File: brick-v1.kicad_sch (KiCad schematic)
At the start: 15 parts, among them J1 battery_header, U1 XBEE S2C PRO, U2 esp32, U3 L7805, U4 ULTRASONIC SENSOR, U5 Teensy4.1

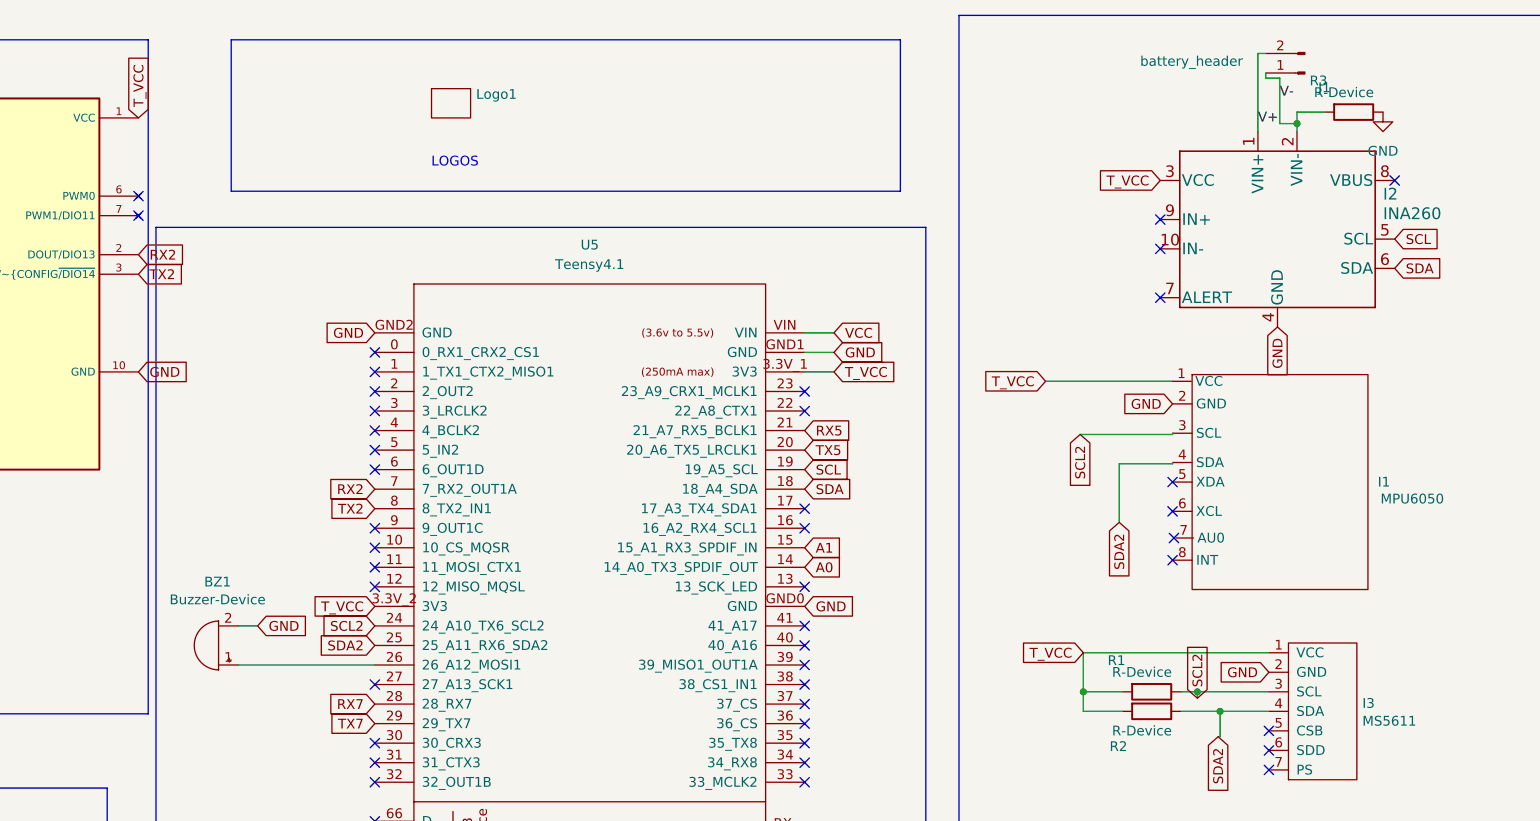
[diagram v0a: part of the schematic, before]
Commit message: fixed ina260 traces
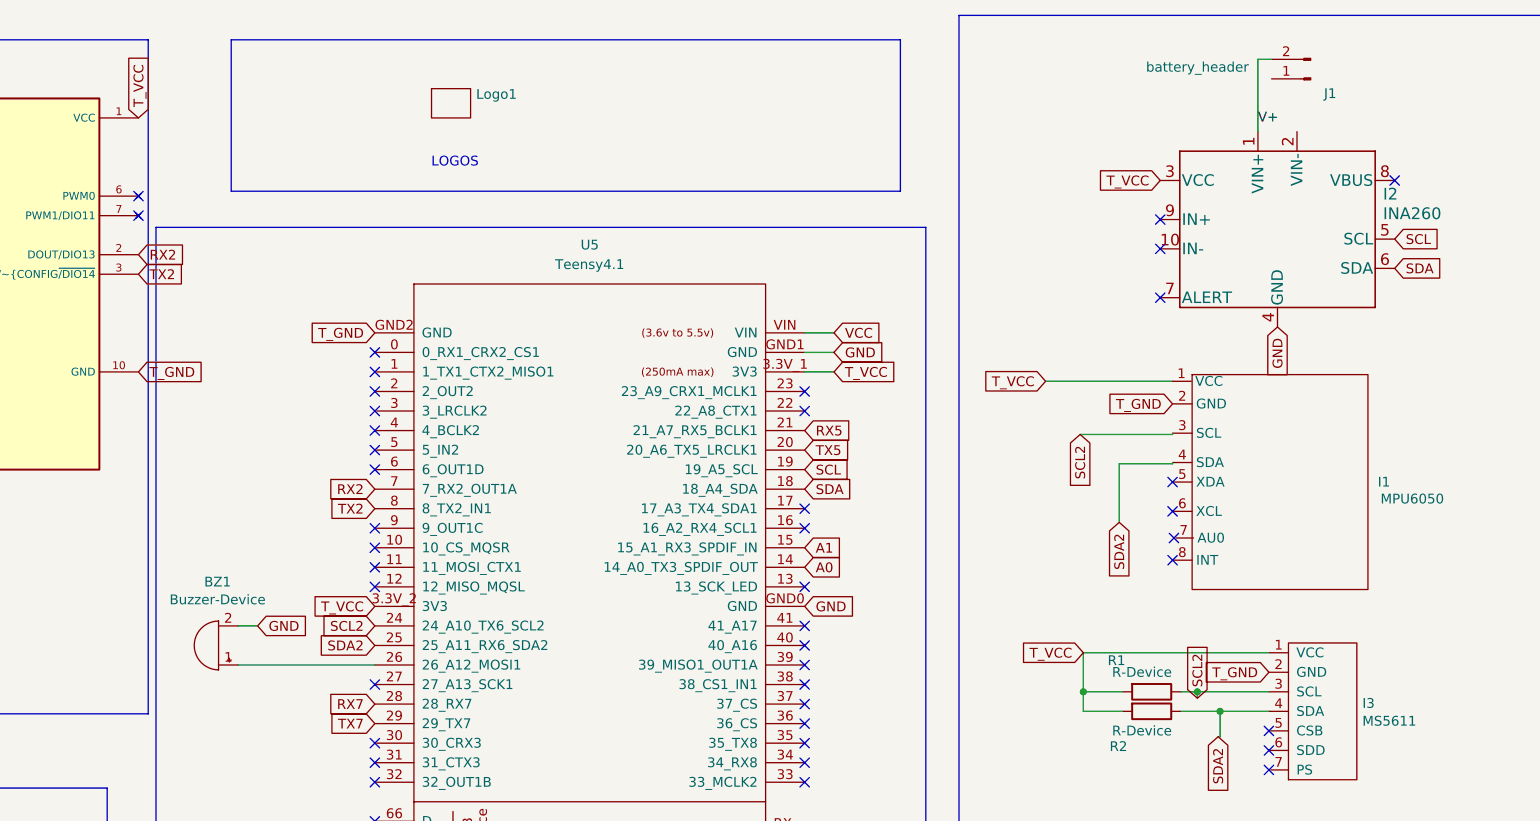
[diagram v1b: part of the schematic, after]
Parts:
- removed R3: R-Device, Resistor_THT:R_Axial_DIN0207_L6.3mm_D2.5mm_P10.16mm_Horizontal, symbol rrc_pcb-rescue:R-Device
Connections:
- net GND: no longer I1.2 (GND), I2.2 (VIN-), I3.2 (GND), J1.1 (Pin_1), U1.10 (GND), U5.GND2 (GND)
- new net T_GND: I1.2 (GND), I3.2 (GND), U1.10 (GND), U5.GND2 (GND)
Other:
- moved on the sheet: J1

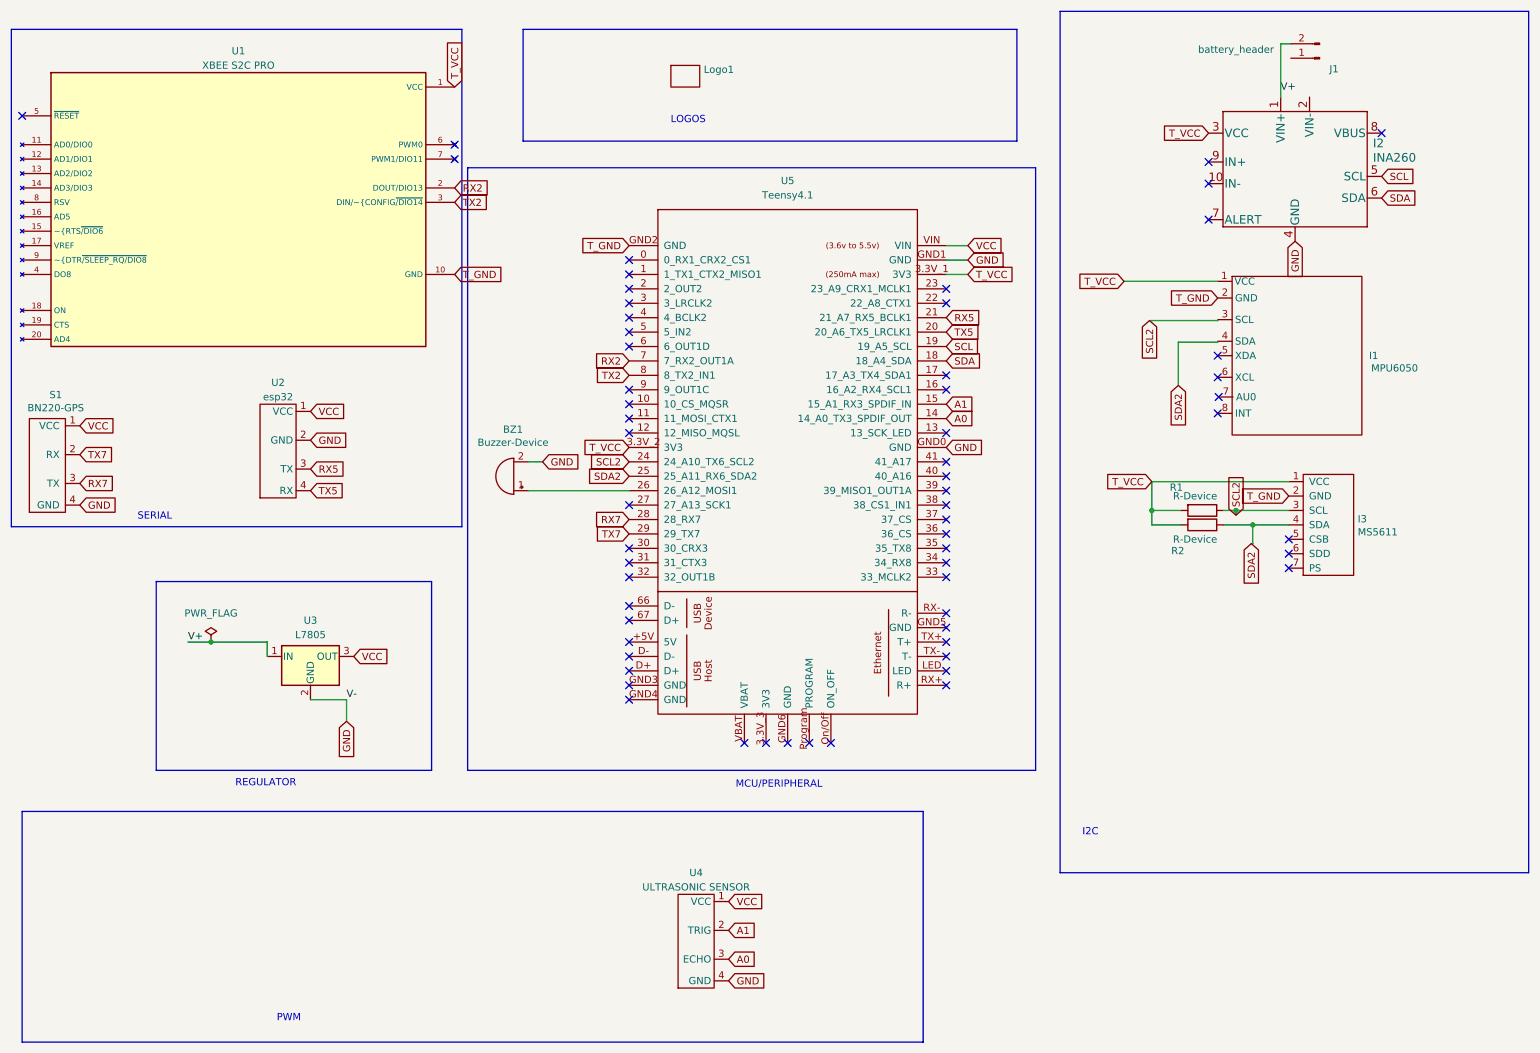
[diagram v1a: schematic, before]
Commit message: changed pcb size and sensor placements
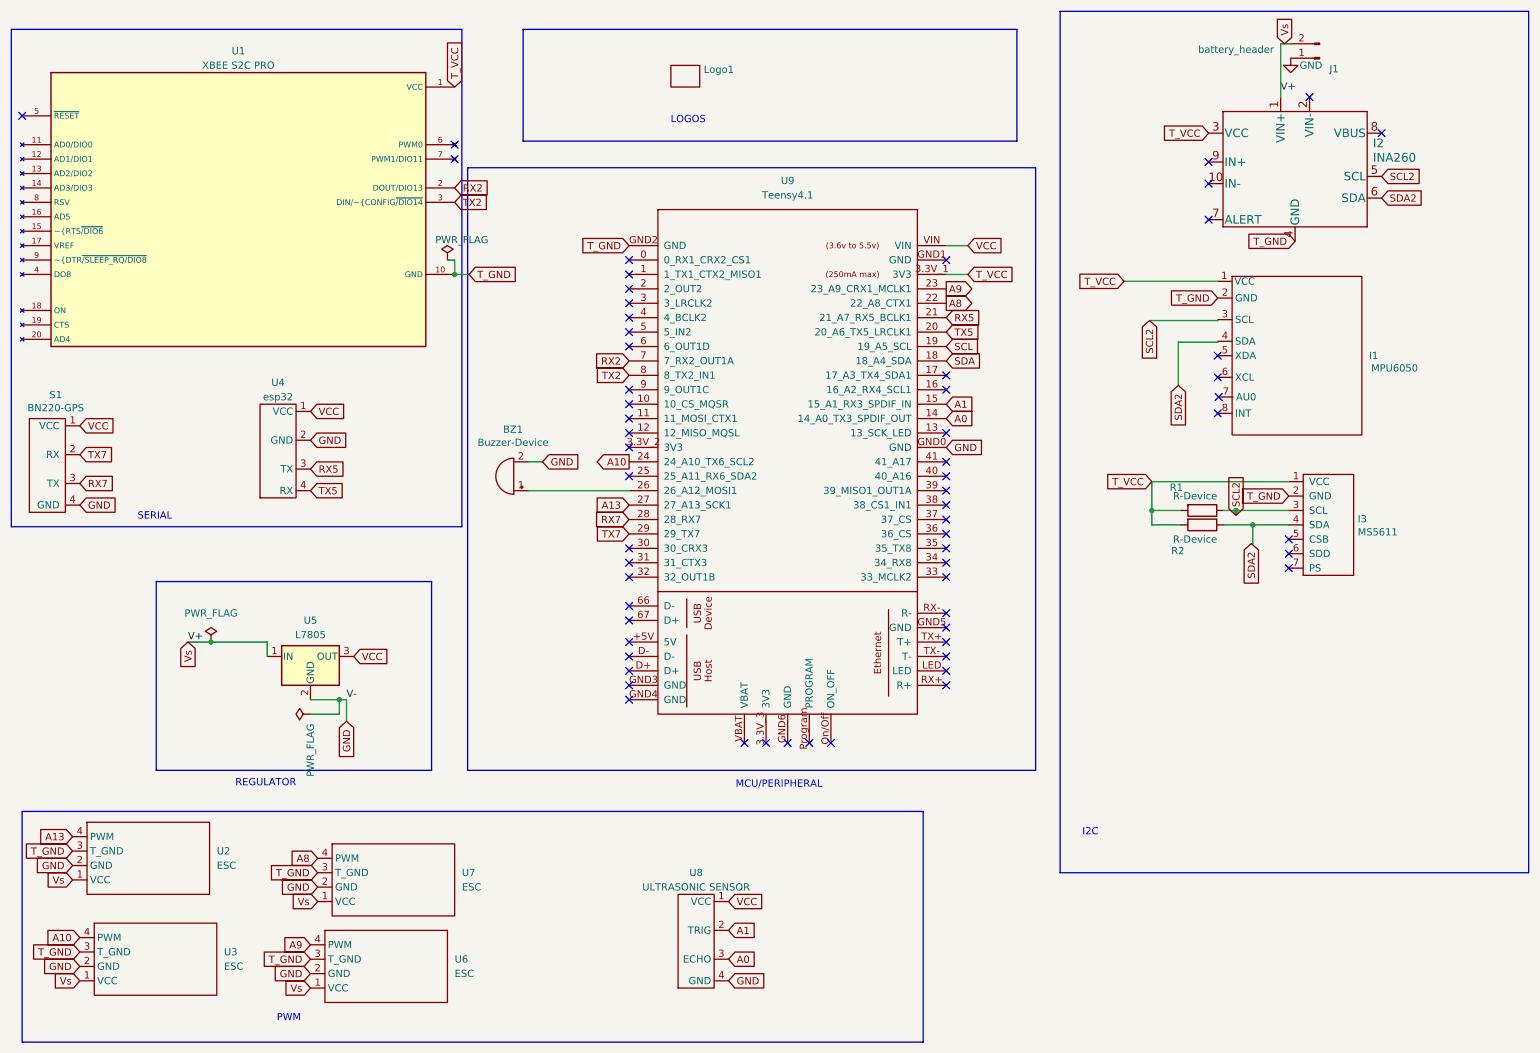
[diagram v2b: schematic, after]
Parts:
- added U2, U3, U6, U7: ESC, RRC_footprint:BLHeLi_esc, symbol parts:ESC
- renumbered U2 to U4, U3 to U5, U4 to U8, U5 to U9
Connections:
- net GND: now also J1.1 (Pin_1), U2.2 (GND), U3.2 (GND), U6.2 (GND), U7.2 (GND); no longer I2.4 (GND), U9.GND1 (GND)
- net SCL: no longer I2.5 (SCL)
- net SCL2: now also I2.5 (SCL); no longer U9.24 (24_A10_TX6_SCL2)
- net SDA: no longer I2.6 (SDA)
- net SDA2: now also I2.6 (SDA); no longer U9.25 (25_A11_RX6_SDA2)
- net T_GND: now also I2.4 (GND), U2.3 (T_GND), U3.3 (T_GND), U6.3 (T_GND), U7.3 (T_GND)
- net T_VCC: no longer U9.3.3V_2 (3V3)
- net A8: now reaches U9.22 (22_A8_CTX1)
- net A8: now also U7.4 (PWM)
- net A9: now reaches U9.23 (23_A9_CRX1_MCLK1)
- net A9: now also U6.4 (PWM)
- net A13: now reaches U9.27 (27_A13_SCK1)
- net A13: now also U2.4 (PWM)
- net V+ renamed Vs
- net Vs: now also U2.1 (VCC), U3.1 (VCC), U6.1 (VCC), U7.1 (VCC)
- new net A10: U3.4 (PWM), U9.24 (24_A10_TX6_SCL2)
- no-connect marks 61 -> 62

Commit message: AC_flight controller updated v1.5
-made 4 layer board
-added esp32 camera
-removed buzzer
-reduced area of pcb
-added TMU logos and my name and other descriptors
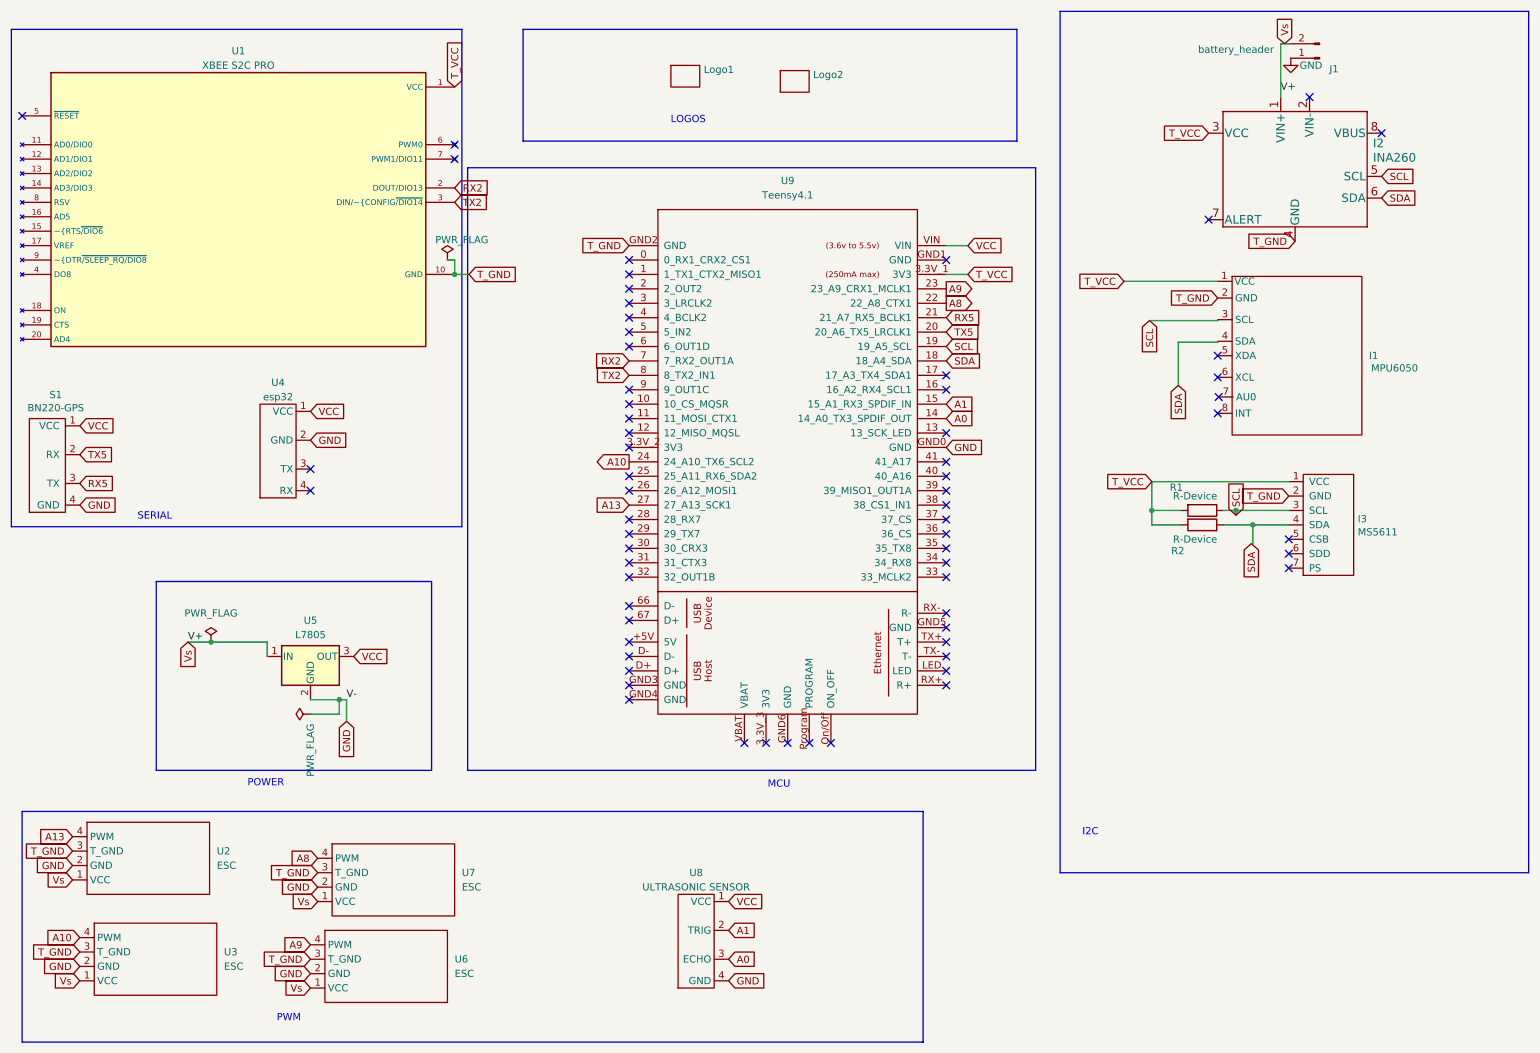
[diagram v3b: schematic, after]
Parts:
- removed BZ1: Buzzer-Device, Buzzer_Beeper:Buzzer_12x9.5RM7.6, symbol rrc_pcb-rescue:Buzzer-Device
- added Logo2: ~, rrc_logo:picturae, symbol rrc_pcb-rescue:logo
- Logo1: footprint rrc_logo:tmu -> rrc_logo:picturae
- S1, U8: footprint rrc_bn220_gps:BN220 -> Connector_PinSocket_2.54mm:PinSocket_1x04_P2.54mm_Vertical
- U4: footprint rrc_bn220_gps:BN220 -> thesis_lib:esp32_cam
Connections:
- net SCL2 is gone; now on net SCL: I1.3 (SCL), I2.5 (SCL), I3.3 (SCL), R1.1
- net SDA2 is gone; now on net SDA: I1.4 (SDA), I2.6 (SDA), I3.4 (SDA), R2.1
- net RX5: now also S1.3 (TX); no longer U4.3 (TX)
- net TX5: now also S1.2 (RX); no longer U4.4 (RX)
- net RX7: no longer names the net of U9.28 (28_RX7)
- net RX7: no longer S1.3 (TX)
- net TX7: no longer names the net of U9.29 (29_TX7)
- net TX7: no longer S1.2 (RX)
- no-connect marks 62 -> 65
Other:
- note added: "MCU"
- note added: "POWER"
- note removed: "MCU/PERIPHERAL"
- note removed: "REGULATOR"
